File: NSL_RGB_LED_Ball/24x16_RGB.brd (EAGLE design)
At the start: 46.4 x 123.7 mm, 95 parts, among them IC1 TLC5947XLP, IC2 TLC5947XLP, IC3 TLC5947XLP, IC4 MEGA8-AI, IC5 MCP73123, IC6 BLUETOOTH-RN41", IC7 MMA7455L, IC8 OPA344, Q2 BSH201, X1 16Mhz

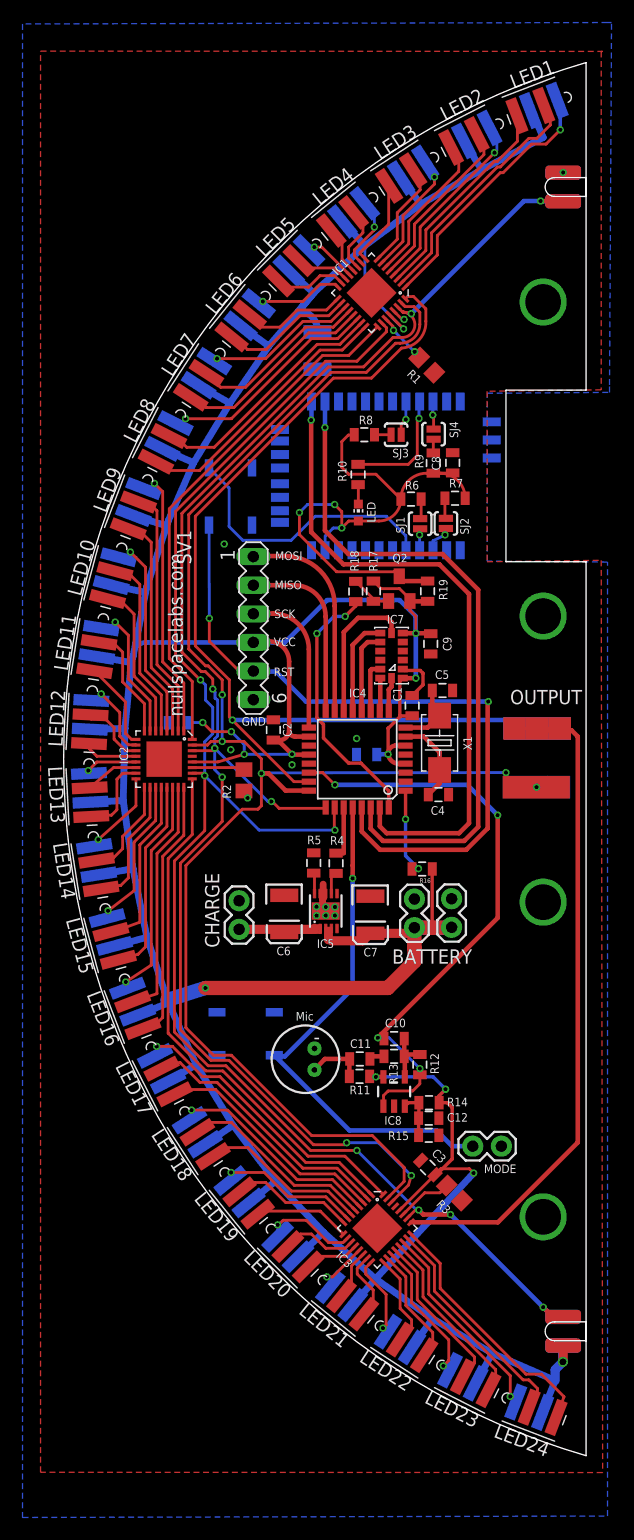
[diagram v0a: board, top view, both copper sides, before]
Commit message: 
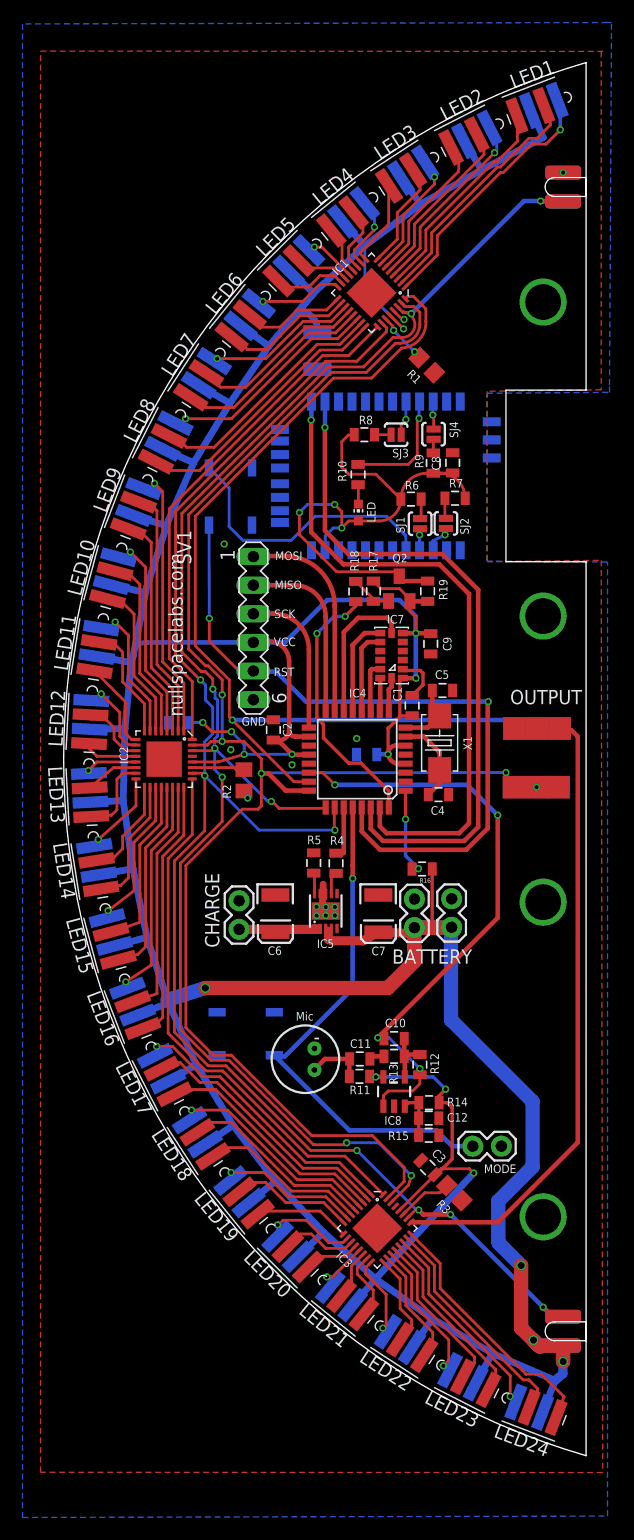
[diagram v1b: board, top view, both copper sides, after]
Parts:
- C9: value (none) -> 0.1uF
- moved C6 0.79 mm to (-45.4, -13.7)
- moved C7 0.72 mm to (-36.2, -13.7)
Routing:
- net VCC: track 419.8 -> 470.5 mm, vias 13 -> 15
- net CHARGE: track 12.5 -> 13.3 mm

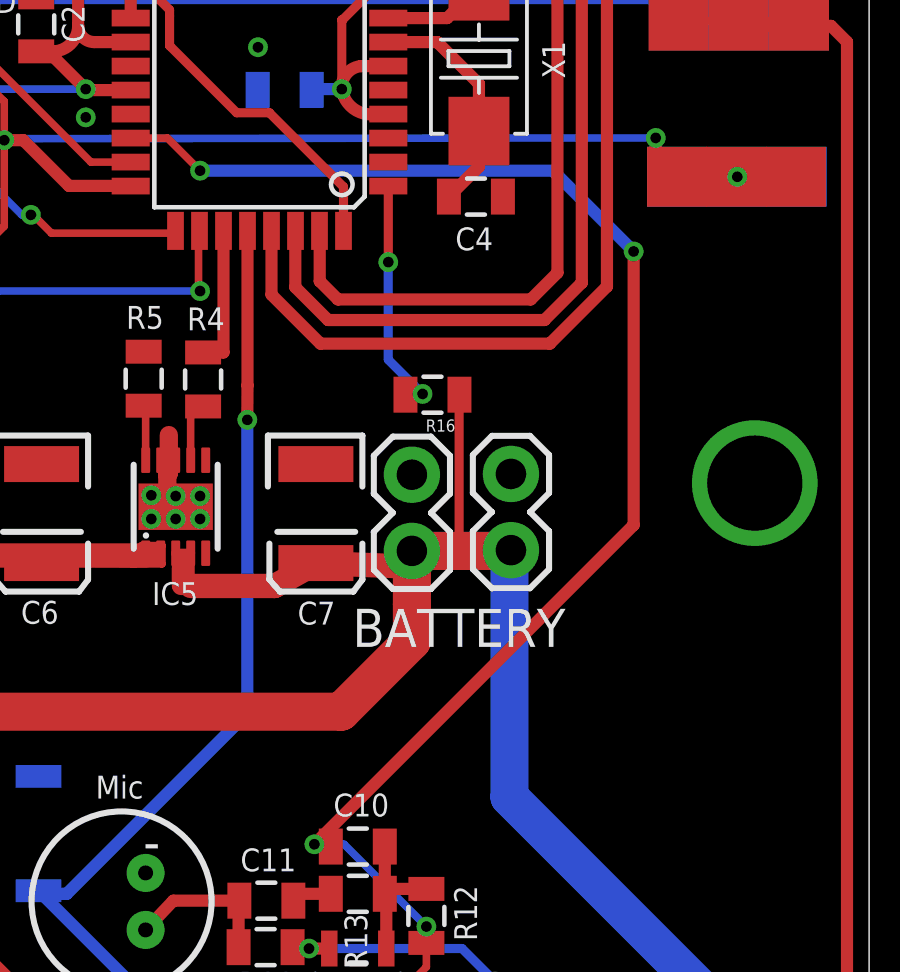
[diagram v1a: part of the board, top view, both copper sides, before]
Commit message: 
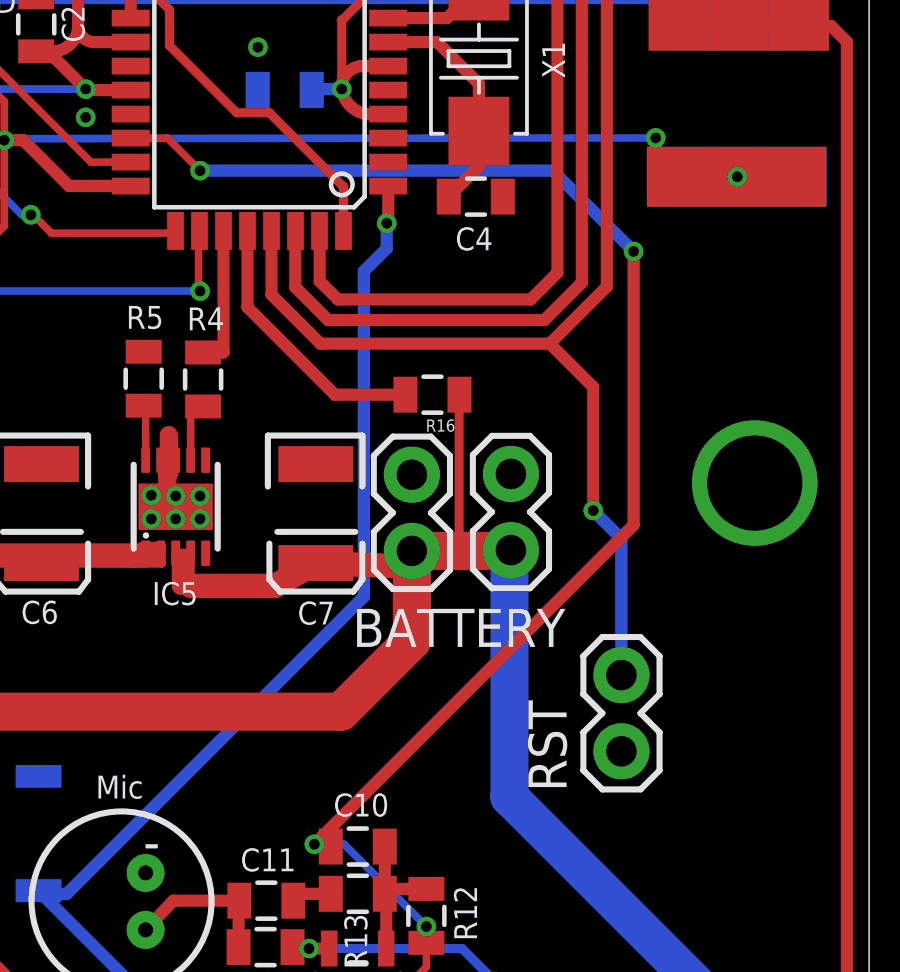
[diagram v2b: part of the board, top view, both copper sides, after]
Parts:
- added RST: (no value), 24x16_RGB:1X02
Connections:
- net BATTSENSE: now also IC4.28; no longer IC4.1
- net BUTTON: now also IC4.1; no longer IC4.28
- net GND: now also RST.1
- net RST: now also RST.2
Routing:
- net RST: track 63.3 -> 75.4 mm, vias 2 -> 3
- net BUTTON: track 46.7 -> 50.1 mm
- net BATTSENSE: track 7.98 -> 9.02 mm, vias 2 -> 0
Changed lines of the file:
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@@
 <attribute name="VALUE" x="-33.2486" y="15.9258" size="0.4064" layer="27" rot="R270"/>
 </element>
+<element name="RST" library="24x16_RGB" package="1X02" value="" x="-26.035" y="-21.6408" rot="R90"/>
 </elements>
 <signals>
@@
 <contactref element="BATTERY1" pad="1"/>
 <via x="-38.1508" y="1.8288" extent="1-16" drill="0.3556"/>
+<contactref element="RST" pad="1"/>
 </signal>
 <signal name="VCC">
@@
 <via x="-26.4668" y="5.1054" extent="1-16" drill="0.3556"/>
 <via x="-51.2318" y="12.4968" extent="1-16" drill="0.3556"/>
+<contactref element="RST" pad="2"/>
+<wire x1="-28.4226" y1="-8.0518" x2="-26.9748" y2="-9.4996" width="0.4064" layer="1"/>
+<wire x1="-26.9748" y1="-9.4996" x2="-26.9748" y2="-13.6144" width="0.4064" layer="1"/>
+<via x="-26.9748" y="-13.6144" extent="1-16" drill="0.3556"/>
+<wire x1="-26.9748" y1="-13.6144" x2="-26.035" y2="-14.5542" width="0.4064" layer="16"/>
+<wire x1="-26.035" y1="-14.5542" x2="-26.035" y2="-19.1008" width="0.4064" layer="16"/>
 </signal>
 <signal name="SCK">
@@
 </signal>
 <signal name="BUTTON">
-<contactref element="IC4" pad="28"/>
 <contactref element="S2" pad="3"/>
-<wire x1="-38.5" y1="-4.2926" x2="-38.5" y2="-9.4424" width="0.4064" layer="1"/>
-<wire x1="-38.5" y1="-9.4424" x2="-38.5064" y2="-10.5918" width="0.4064" layer="1"/>
-<wire x1="-38.5064" y1="-10.5918" x2="-38.5064" y2="-20.3708" width="0.4064" layer="16"/>
 <wire x1="-38.5064" y1="-20.3708" x2="-44.5262" y2="-26.3906" width="0.4064" layer="16"/>
 <wire x1="-44.5262" y1="-26.3906" x2="-45.5168" y2="-26.3906" width="0.4064" layer="16"/>
@@
 <wire x1="-38.7858" y1="-32.9692" x2="-31.0642" y2="-32.9692" width="0.4064" layer="16"/>
 <wire x1="-31.0642" y1="-32.9692" x2="-29.6672" y2="-34.3662" width="0.4064" layer="16"/>
-<via x="-38.5064" y="-10.5918" extent="1-16" drill="0.3556"/>
 <contactref element="MODE" pad="2"/>
 <wire x1="-29.6672" y1="-34.3662" x2="-27.8384" y2="-34.3662" width="0.4064" layer="16"/>
+<contactref element="IC4" pad="1"/>
+<wire x1="-38.5064" y1="-20.3708" x2="-34.6202" y2="-16.4846" width="0.4064" layer="16"/>
+<wire x1="-34.6202" y1="-16.4846" x2="-34.6202" y2="-5.6388" width="0.4064" layer="16"/>
+<wire x1="-34.6202" y1="-5.6388" x2="-33.8582" y2="-4.8768" width="0.4064" layer="16"/>
+<wire x1="-33.8582" y1="-4.8768" x2="-33.8582" y2="-4.0386" width="0.4064" layer="16"/>
+<via x="-33.8582" y="-4.0386" extent="1-16" drill="0.3556"/>
+<wire x1="-33.8582" y1="-4.0386" x2="-33.8074" y2="-3.9878" width="0.4064" layer="1"/>
+<wire x1="-33.8074" y1="-3.9878" x2="-33.8074" y2="-2.8" width="0.4064" layer="1"/>
 </signal>
 <signal name="TX">
@@
 </signal>
 <signal name="BATTSENSE">
-<contactref element="IC4" pad="1"/>
 <contactref element="R16" pad="2"/>
-<wire x1="-33.8074" y1="-2.8" x2="-33.8074" y2="-5.334" width="0.3048" layer="1"/>
-<via x="-33.8074" y="-5.334" extent="1-16" drill="0.3556"/>
-<wire x1="-33.8074" y1="-5.334" x2="-33.8074" y2="-8.5852" width="0.3048" layer="16"/>
-<wire x1="-33.8074" y1="-8.5852" x2="-32.6644" y2="-9.7282" width="0.3048" layer="16"/>
-<via x="-32.6644" y="-9.7282" extent="1-16" drill="0.3556"/>
-<wire x1="-32.6644" y1="-9.7282" x2="-33.2088" y2="-9.7282" width="0.3048" layer="1"/>
-<wire x1="-33.2088" y1="-9.7282" x2="-33.2342" y2="-9.7536" width="0.3048" layer="1"/>
+<contactref element="IC4" pad="28"/>
+<wire x1="-38.5" y1="-4.2926" x2="-38.5" y2="-6.839" width="0.4064" layer="1"/>
+<wire x1="-38.5" y1="-6.839" x2="-35.5854" y2="-9.7536" width="0.4064" layer="1"/>
+<wire x1="-35.5854" y1="-9.7536" x2="-33.2342" y2="-9.7536" width="0.4064" layer="1"/>
 </signal>
 <signal name="VDD">

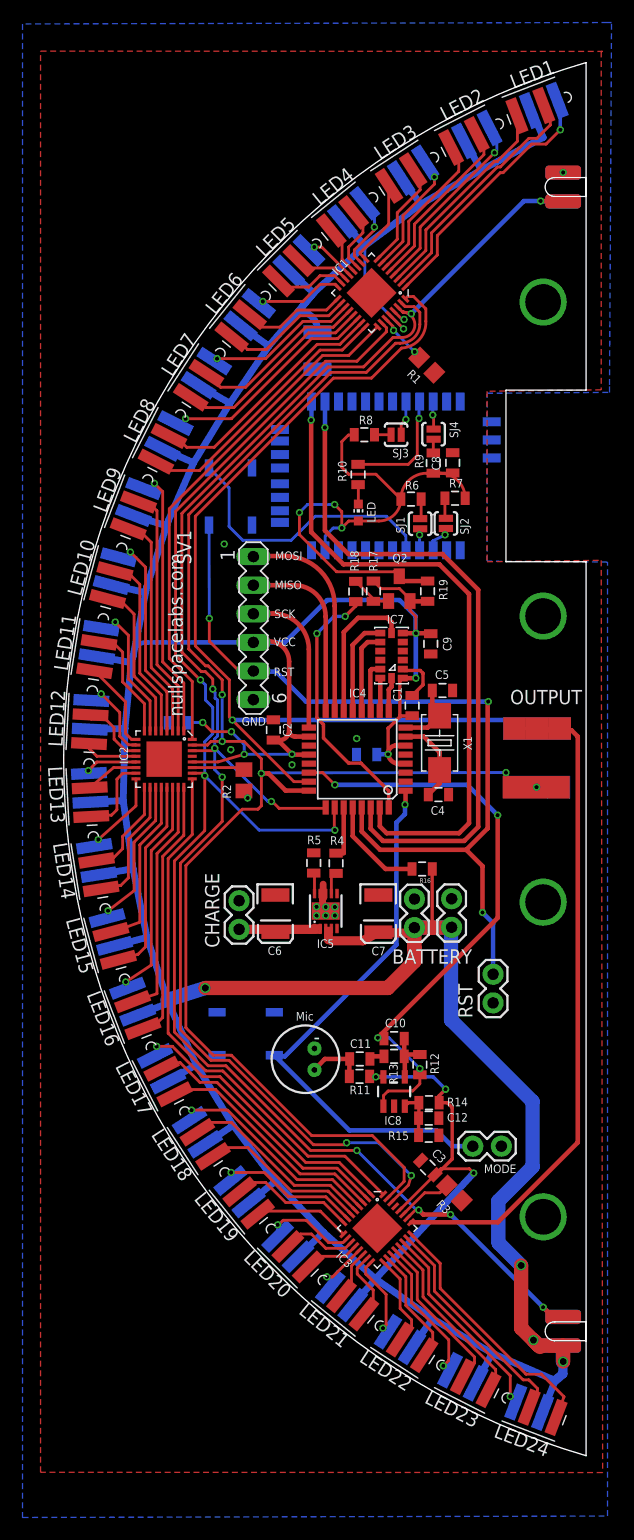
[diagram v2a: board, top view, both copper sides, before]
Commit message: 
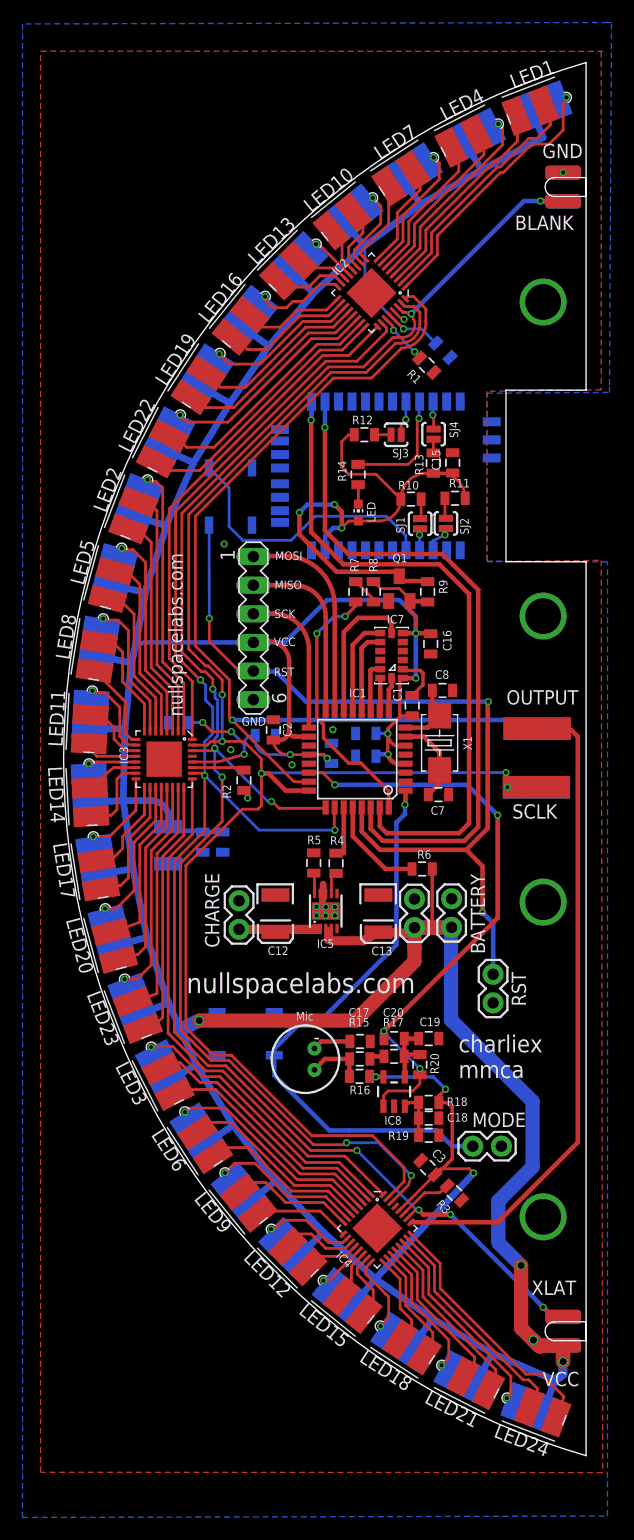
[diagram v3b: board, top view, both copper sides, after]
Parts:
- added C13: 4.7uF, slice_noshift:EIA3528
- added C17: 4.7uF, SparkFun:0805
- added C18: 1uF, SparkFun:0805
- added C19: .1uF, SparkFun:0805
- added C20: 12pF, SparkFun:0805
- added C21, C22: 1uF, 24x16_RGB:0805
- added R20: 1M, SparkFun:0805
- C10: value 100pF -> .1uF; device SparkFun:0805 -> slice_noshift:0805
- C11: device SparkFun:0805 -> slice_noshift:0805
- C12: value 1uF -> 4.7uF; device SparkFun:0805 -> slice_noshift:EIA3528
- C14: value .1uF -> 47uF; device slice_noshift:0805 -> slice_noshift:EIA3528
- C15: device slice_noshift:0805 -> SparkFun:0805
- C16: value 4.7uF -> 0.1uF; device slice_noshift:EIA3528 -> SparkFun:0805
- C4, C5: value 18pF -> .1uF
- C6: value 4.7uF -> .1uF; device slice_noshift:EIA3528 -> slice_noshift:0805
- C7: value 4.7uF -> 18pF; device slice_noshift:EIA3528 -> slice_noshift:0805
- C8: value .1uF -> 18pF; device SparkFun:0805 -> slice_noshift:0805
- C9: value 0.1uF -> .1uF; device SparkFun:0805 -> slice_noshift:0805
- IC1: value TLC5947XLP -> MEGA8-AI; device slice_noshift:QFN32_XLP -> atmel:TQFP32-08
- IC4: value MEGA8-AI -> TLC5947XLP; device atmel:TQFP32-08 -> slice_noshift:QFN32_XLP
- R1, R2, R3: device rcl:R0805 -> 24x16_RGB:0805
- R10: value 220 -> 1k
- R11: value 2.2k -> 1k
- R12: value 100K -> 1k
- R14: value 10k -> 220
- R15: value 10k -> 4.7k
- R16: value 220K -> 2.2k; device slice_noshift:0805 -> SparkFun:0805
- R19: value 0ohm DNP -> 10k
- R6: value 1k -> 220K; device SparkFun:0805 -> slice_noshift:0805
- R7, R8: value 1k -> 10k
- R9: value 1k -> 0ohm DNP
- moved LED3 85.0 mm to (-56.6, -28.8), turned to 117 degrees
- moved LED22 84.9 mm to (-56.6, 28.8), turned to 63 degrees
- moved LED6 74.6 mm to (-53.3, -34.6), turned to 123 degrees
- moved LED19 74.6 mm to (-53.2, 34.6), turned to 57 degrees
- moved LED9 63.5 mm to (-49.3, -40.0), turned to 129 degrees
- moved LED16 63.5 mm to (-49.3, 39.9), turned to 51 degrees
- moved C11 63.4 mm to (-30.5, 36.3), flipped to the bottom, turned to 225 degrees
- moved R12 56.1 mm to (-37.5, 28.8), turned to 180 degrees
- moved R14 56.1 mm to (-38.0, 25.3), turned to 270 degrees
- moved R13 52.8 mm to (-31.3, 26.3), turned to 270 degrees
- moved R11 52.0 mm to (-29.4, 23.2)
- moved LED12 51.7 mm to (-44.9, -44.9), turned to 135 degrees
- moved LED13 51.7 mm to (-44.9, 44.9), turned to 45 degrees
- moved R19 48.3 mm to (-31.8, -33.4), turned to 0 degrees
- moved R18 45.8 mm to (-31.8, -30.5), turned to 0 degrees
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- renumbered Q2 to Q1
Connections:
- removed net N$3 (its old number): IC1.25, IC2.32
- removed net VSENSE: IC4.19
- new net N$19: IC3.25, IC4.32
- new net N$20: MIC1.2, R15.2
- net !CS: now also IC1.14; no longer IC4.14
- net BATTSENSE: now also IC1.28, R6.2; no longer IC4.28, R16.2
- net BLANK: now also IC1.25, IC4.30; no longer IC1.30, IC4.25
- net BT_PWR: now also IC1.32, R7.2; no longer IC4.32, R18.2
- net BUTTON: now also IC1.1; no longer IC4.1
- net CHARGE: now also C12.A; no longer C6.A
- net COL1: now also IC2.1; no longer IC1.1
- net COL10: now also IC2.10, LED10.B; no longer IC1.10, LED4.B
- net COL11: now also IC2.11, LED10.G; no longer IC1.11, LED4.G
- net COL12: now also IC2.12, LED10.R; no longer IC1.12, LED4.R
- net COL13: now also IC2.13, LED13.B; no longer IC1.13, LED5.B
- net COL14: now also IC2.14, LED13.G; no longer IC1.14, LED5.G
- net COL15: now also IC2.15, LED13.R; no longer IC1.15, LED5.R
- net COL16: now also IC2.16, LED16.B; no longer IC1.16, LED6.B
- net COL17: now also IC2.17, LED16.G; no longer IC1.17, LED6.G
- net COL18: now also IC2.18, LED16.R; no longer IC1.18, LED6.R
- net COL19: now also IC2.19, LED19.B; no longer IC1.19, LED7.B
- net COL2: now also IC2.2; no longer IC1.2
- net COL20: now also IC2.20, LED19.G; no longer IC1.20, LED7.G
- net COL21: now also IC2.21, LED19.R; no longer IC1.21, LED7.R
- net COL22: now also IC2.22, LED22.B; no longer IC1.22, LED8.B
- net COL23: now also IC2.23, LED22.G; no longer IC1.23, LED8.G
- net COL24: now also IC2.24, LED22.R; no longer IC1.24, LED8.R
- net COL25: now also IC3.1, LED2.B; no longer IC2.1, LED9.B
- net COL26: now also IC3.2, LED2.G; no longer IC2.2, LED9.G
- net COL27: now also IC3.3, LED2.R; no longer IC2.3, LED9.R
- net COL28: now also IC3.4, LED5.B; no longer IC2.4, LED10.B
- net COL29: now also IC3.5, LED5.G; no longer IC2.5, LED10.G
- net COL3: now also IC2.3; no longer IC1.3
- net COL30: now also IC3.6, LED5.R; no longer IC2.6, LED10.R
- net COL31: now also IC3.7, LED8.B; no longer IC2.7, LED11.B
- net COL32: now also IC3.8, LED8.G; no longer IC2.8, LED11.G
- net COL33: now also IC3.9, LED8.R; no longer IC2.9, LED11.R
- net COL34: now also IC3.10, LED11.B; no longer IC2.10, LED12.B
- net COL35: now also IC3.11, LED11.G; no longer IC2.11, LED12.G
- net COL36: now also IC3.12, LED11.R; no longer IC2.12, LED12.R
- net COL37: now also IC3.13, LED14.B; no longer IC2.13, LED13.B
- net COL38: now also IC3.14, LED14.G; no longer IC2.14, LED13.G
- net COL39: now also IC3.15, LED14.R; no longer IC2.15, LED13.R
- net COL4: now also IC2.4, LED4.B; no longer IC1.4, LED2.B
- net COL40: now also IC3.16, LED17.B; no longer IC2.16, LED14.B
- net COL41: now also IC3.17, LED17.G; no longer IC2.17, LED14.G
- net COL42: now also IC3.18, LED17.R; no longer IC2.18, LED14.R
- net COL43: now also IC3.19, LED20.B; no longer IC2.19, LED15.B
- net COL44: now also IC3.20, LED20.G; no longer IC2.20, LED15.G
- net COL45: now also IC3.21, LED20.R; no longer IC2.21, LED15.R
- net COL46: now also IC3.22, LED23.B; no longer IC2.22, LED16.B
- net COL47: now also IC3.23, LED23.G; no longer IC2.23, LED16.G
- net COL48: now also IC3.24, LED23.R; no longer IC2.24, LED16.R
- net COL49: now also IC4.1, LED3.B; no longer IC3.1, LED17.B
- net COL5: now also IC2.5, LED4.G; no longer IC1.5, LED2.G
- net COL50: now also IC4.2, LED3.G; no longer IC3.2, LED17.G
- net COL51: now also IC4.3, LED3.R; no longer IC3.3, LED17.R
- net COL52: now also IC4.4, LED6.B; no longer IC3.4, LED18.B
- net COL53: now also IC4.5, LED6.G; no longer IC3.5, LED18.G
- net COL54: now also IC4.6, LED6.R; no longer IC3.6, LED18.R
- net COL55: now also IC4.7, LED9.B; no longer IC3.7, LED19.B
- net COL56: now also IC4.8, LED9.G; no longer IC3.8, LED19.G
- net COL57: now also IC4.9, LED9.R; no longer IC3.9, LED19.R
- net COL58: now also IC4.10, LED12.B; no longer IC3.10, LED20.B
- net COL59: now also IC4.11, LED12.G; no longer IC3.11, LED20.G
- net COL6: now also IC2.6, LED4.R; no longer IC1.6, LED2.R
- net COL60: now also IC4.12, LED12.R; no longer IC3.12, LED20.R
- net COL61: now also IC4.13, LED15.B; no longer IC3.13, LED21.B
- net COL62: now also IC4.14, LED15.G; no longer IC3.14, LED21.G
- net COL63: now also IC4.15, LED15.R; no longer IC3.15, LED21.R
- net COL64: now also IC4.16, LED18.B; no longer IC3.16, LED22.B
- net COL65: now also IC4.17, LED18.G; no longer IC3.17, LED22.G
- net COL66: now also IC4.18, LED18.R; no longer IC3.18, LED22.R
- net COL67: now also IC4.19, LED21.B; no longer IC3.19, LED23.B
- net COL68: now also IC4.20, LED21.G; no longer IC3.20, LED23.G
- net COL69: now also IC4.21, LED21.R; no longer IC3.21, LED23.R
- net COL7: now also IC2.7, LED7.B; no longer IC1.7, LED3.B
- net COL70: now also IC4.22; no longer IC3.22
- net COL71: now also IC4.23; no longer IC3.23
- net COL72: now also IC4.24; no longer IC3.24
- net COL8: now also IC2.8, LED7.G; no longer IC1.8, LED3.G
- net COL9: now also IC2.9, LED7.R; no longer IC1.9, LED3.R
- net GND: now also C10.2, C11.2, C12.C, C13.C, C14.C, C16.1, C18.1, C19.2, C21.2, C22.2, C6.2, C7.2, C9.2, IC1.21, IC1.3, IC1.5, IC4.29, R15.1, R19.2; no longer C12.1, C14.2, C16.C, C6.C, C7.C, C9.1, IC1.29, IC4.21, IC4.3, IC4.5, MIC1.2, R15.2
- net HOLE: now also IC2.27; no longer IC1.27
- net INT1/DRDY: now also IC1.13; no longer IC4.13
- net INT2: now also IC1.12; no longer IC4.12
- net MIC: now also C20.1, IC1.22, R20.2; no longer C10.1, IC4.22, R12.2
- net MISO: now also IC1.16; no longer IC4.16
- net MOSI: now also IC1.15; no longer IC4.15
- net N$14: now also C17.2, R17.2; no longer C11.2, R13.2
- net N$15: now also C17.1, R16.1; no longer C11.1, R11.1
- net N$16: now also C18.2, R18.1, R19.1; no longer C12.2, R14.1, R15.1
- net N$17: now also C19.1, C20.2, R17.1, R20.1; no longer C10.2, R12.1, R13.1
- net N$18: now also R7.1, R8.1; no longer R17.1, R18.1
- net N$2: now also IC3.27; no longer IC2.27
- net N$21: now also R12.1; no longer R8.1
- net N$23: now also R11.1; no longer R7.1
- net N$24: now also R13.1; no longer R9.1
- net N$4: now also R14.2; no longer R10.2
- net N$5: now also R10.1; no longer R6.1
- net N$7: now also C7.1, IC1.7; no longer C4.1, IC4.7
- net N$8: now also C8.1, IC1.8; no longer C5.1, IC4.8
- net N$9: now also IC4.27; no longer IC3.27
- net PIO5: now also R14.1; no longer R10.1
- net RST: now also IC1.29; no longer IC4.29
- net RX: now also IC1.30; no longer IC4.30
- net SCK: now also IC1.17; no longer IC4.17
- net SCL/SPC: now also IC1.10; no longer IC4.10
- net SCLK: now also IC1.24, IC4.31; no longer IC1.31, IC4.24
- net SDA/SDI/SDO: now also IC1.11; no longer IC4.11
- net SDO: now also IC1.9; no longer IC4.9
- net SIN: now also IC1.23, IC2.32; no longer IC1.32, IC4.23
- net SOUT: now also IC4.25; no longer IC3.25
- net STAT: now also IC1.27; no longer IC4.27
- net TX: now also IC1.31; no longer IC4.31
- net VCC: now also C10.1, C11.1, C13.A, C14.A, C16.2, C21.1, C22.1, C4.1, C5.1, C6.1, C9.1, IC1.18, IC1.20, IC1.4, IC1.6, IC4.28, R16.2, R18.2, R6.1, R8.2, R9.2; no longer C14.1, C15.1, C16.A, C7.A, C9.2, IC1.28, IC4.18, IC4.20, IC4.4, IC4.6, R11.2, R14.2, R16.1, R17.2, R19.2
- net VDD: now also C15.1, R10.2, R11.2, R12.2, R13.2, R9.1; no longer C8.1, R19.1, R6.2, R7.2, R8.2, R9.2
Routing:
- net N$19: track 0.00 -> 48.5 mm
- net N$3 (its old number): track 46.5 -> 0.00 mm
- net VCC: track 470.5 -> 488.0 mm, vias 15 -> 17
- net SCLK: track 154.3 -> 158.1 mm
- net COL10: track 6.65 -> 10.2 mm
- net N$20: track 0.00 -> 3.41 mm
- net COL4: track 17.1 -> 19.5 mm
- net N$3: track 48.5 -> 46.5 mm
- net COL7: track 11.4 -> 13.4 mm
- net COL31: track 12.4 -> 14.1 mm
- net COL1: track 23.3 -> 24.9 mm
- net COL55: track 12.8 -> 14.1 mm
- net COL28: track 18.5 -> 19.8 mm
- net BUTTON: track 50.1 -> 51.4 mm
- net N$17: track 4.87 -> 6.15 mm
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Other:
- board text added: "BLANK"
- board text added: "SCLK"
- board text added: "XLAT"
- board text added: "charliex mmca"
